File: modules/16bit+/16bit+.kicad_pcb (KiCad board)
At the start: 2 copper layers, 30.5 x 68.6 mm, 77 parts, among them J1 Conn_01x08_Socket, J2 Conn_01x08_Socket, J5 USB_C_Receptacle_USB2.0_14P, SW1 K2-1808SN-A4SW-01, SW2 K2-1808SN-A4SW-01, SW3 K2-1808SN-A4SW-01, U1 RP2350_60QFN, U2 W25Q128JVS, U3 MCP6002-xSN, U5 PSRAM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

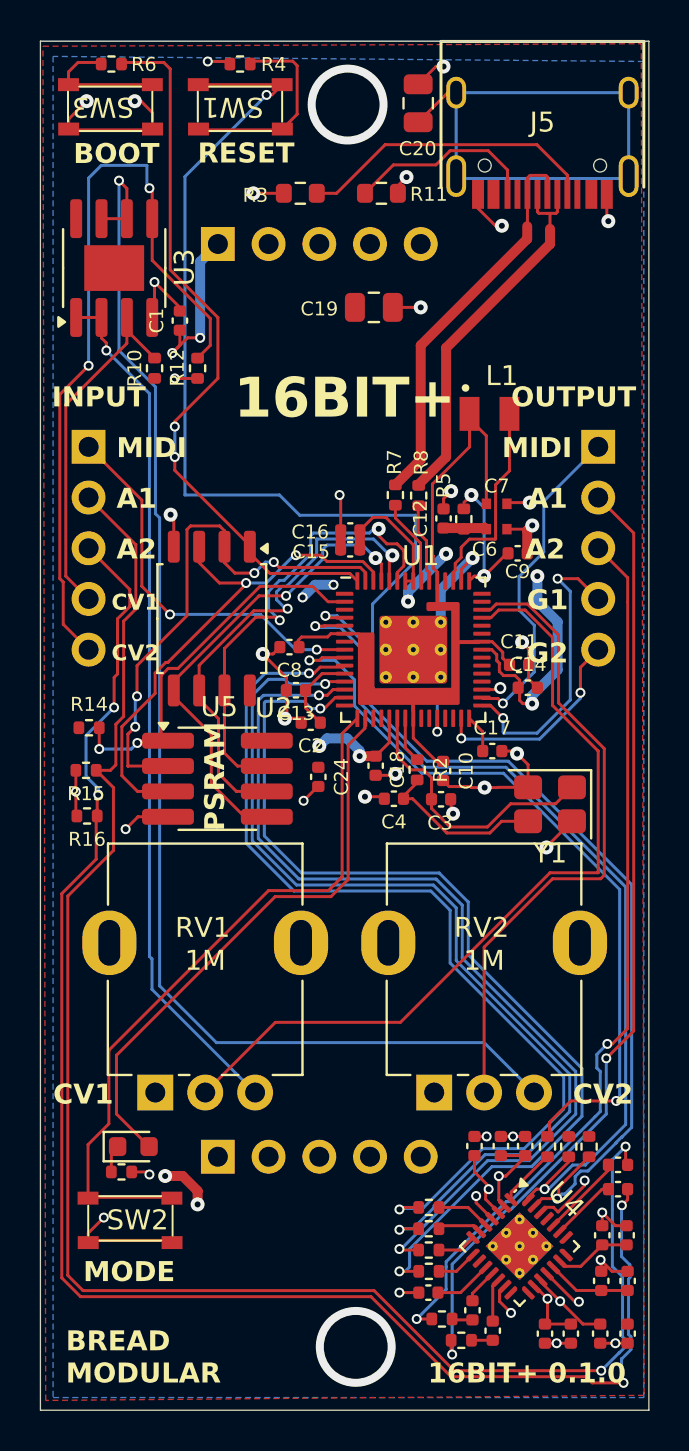
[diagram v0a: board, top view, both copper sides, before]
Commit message: 16bit+: add external crystal to generate MCLK
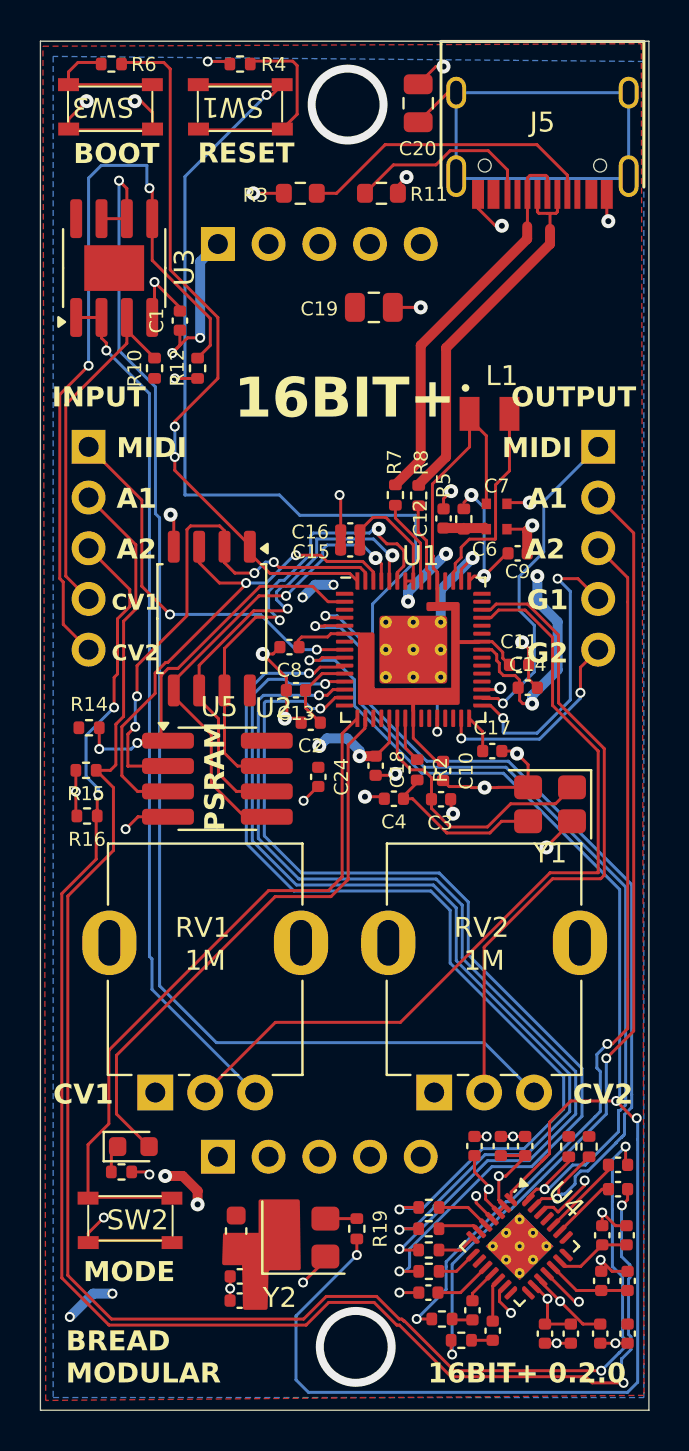
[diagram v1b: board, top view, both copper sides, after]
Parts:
- added C28: 100nf, Capacitor_SMD:C_0402_1005Metric, F.Cu at (57.0, 102.5)
- added C29: 1uf, Capacitor_SMD:C_0402_1005Metric, F.Cu at (57.0, 103.7)
- added FB3: BLM18AG601SN1D, Capacitor_SMD:C_0603_1608Metric, F.Cu at (56.8, 100.2)
- added Y2: SX3M11.2896M20F30TNN, Oscillator:Oscillator_SMD_SiT_PQFN-4Pin_3.2x2.5mm, F.Cu at (60.2, 100.6)
- moved R19 10.4 mm to (62.8, 100.1)
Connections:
- R19 pad 1: MCLK -> Net-(Y2-OUT)
- R19 pad 2: Net-(U4-MCLK) -> MCLK
- U4 pad 1: Net-(U4-MCLK) -> MCLK
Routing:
- net MCLK: track 38.0 -> 82.9 mm, vias 2 -> 4
- net Net-(Y2-OE): track 0.00 -> 7.43 mm
- net Net-(U4-MCLK): track 3.04 -> 0.00 mm
- net GND: track 101.3 -> 104.2 mm, vias 42 -> 44
- net +3V3: track 65.9 -> 68.5 mm, vias 17 -> 19
- net Net-(Y2-OUT): track 0.00 -> 1.57 mm
- net AIN_1: track 84.5 -> 85.4 mm
- net AIN_2: track 80.0 -> 80.9 mm
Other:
- board text added: "16BIT+ 0.2.0"
- board text removed: "16BIT+ 0.1.0"
